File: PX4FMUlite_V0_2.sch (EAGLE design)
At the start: 148 parts, among them J201 DF13C-6P-1.25V, J202 DF13C-6P-1.25V, J203 DF13C-6P-1.25V, J204 DF13C-6P-1.25V, J301 47346-0001, J302 DF13C-4P-1.25V, J401 DF13C-4P-1.25V, J403 DF13C-7P-1.25V, J404 DF13C-5P-1.25V, J405 DF13C-4P-1.25V, J702 DF13C-3P-1.25V, J801 JST-ZH-3, M3_MOUNT1101 MOUNT-HOLE3.1MM, M3_MOUNT1102 MOUNT-HOLE3.1MM, M3_MOUNT1103 MOUNT-HOLE3.1MM, M3_MOUNT1104 MOUNT-HOLE3.1MM, U1 MPU-6000QFN-24, U101 STM32F4X7VX, U401 MAX3051, U903 74LVC2G240, X101 3.2x2.5 mm / 24 MHz / 15 ppm

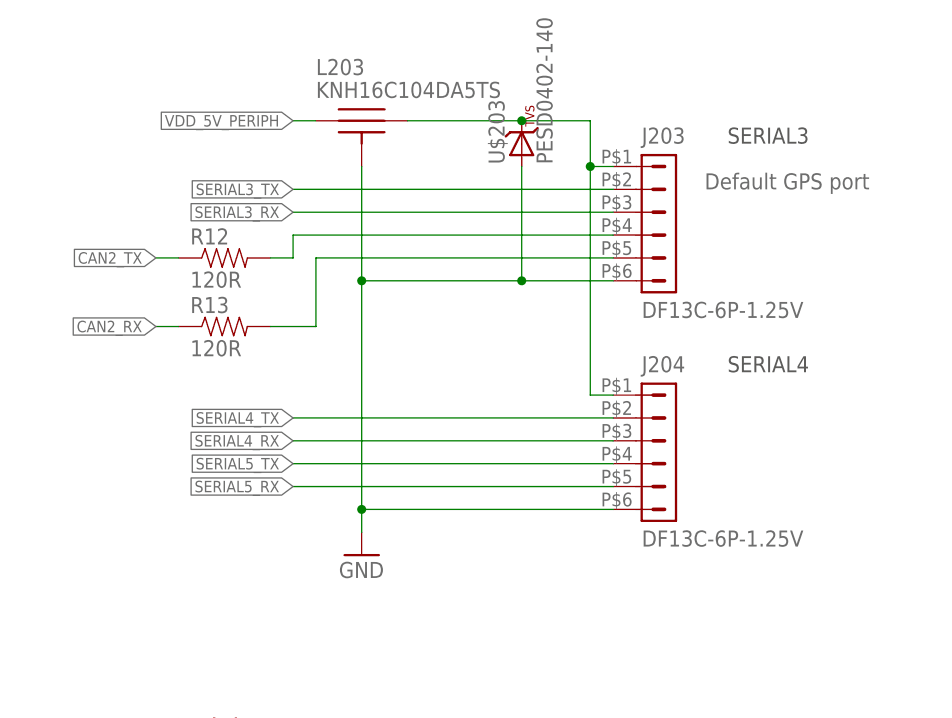
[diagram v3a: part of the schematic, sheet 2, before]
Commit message: Removed excess UART4/5 connector
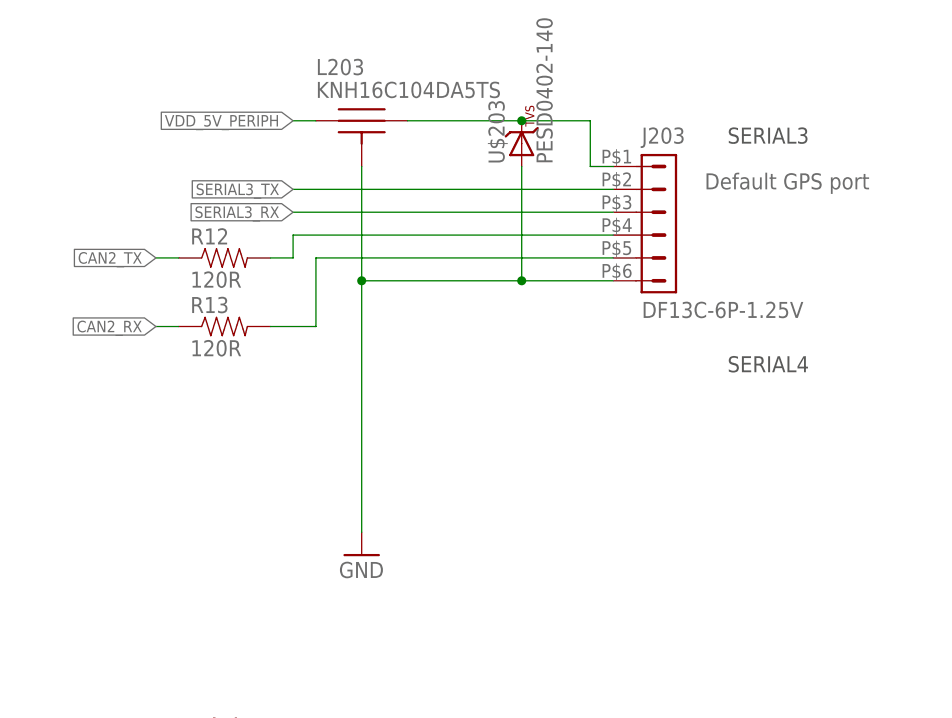
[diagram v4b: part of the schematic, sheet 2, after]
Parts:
- removed J204: DF13C-6P-1.25V, con-hirose-df13:DF13-6P-1.25V
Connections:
- net GNDX: no longer J204.6
- net N$100: no longer J204.1
- net SERIAL4_RX: no longer J204.3
- net SERIAL4_TX: no longer J204.2
- net SERIAL5_RX: no longer J204.5
- net SERIAL5_TX: no longer J204.4
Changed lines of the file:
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@@
-<attribute name="PARTNO" value="DF13C-6P-1.25V(20)"/>
-</part>
-<part name="J204" library="con-hirose-df13" deviceset="DF13-6P-1.25" device="V" value="DF13C-6P-1.25V">
 <attribute name="PARTNO" value="DF13C-6P-1.25V(20)"/>
 </part>
@@
 <attribute name="PARTNO" x="226.06" y="114.3" size="1.778" layer="96" display="off"/>
 </instance>
-<instance part="J204" gate="G$1" x="226.06" y="50.8">
-<attribute name="PARTNO" x="226.06" y="50.8" size="1.778" layer="96" display="off"/>
-</instance>
 <instance part="GND10" gate="1" x="193.04" y="38.1"/>
 <instance part="L201" gate="G$1" x="193.04" y="157.48">
@@
 <wire x1="220.98" y1="68.58" x2="210.82" y2="68.58" width="0.1524" layer="91"/>
 <pinref part="J203" gate="G$1" pin="6"/>
-<pinref part="J204" gate="G$1" pin="6"/>
 <wire x1="210.82" y1="68.58" x2="193.04" y2="68.58" width="0.1524" layer="91"/>
-<wire x1="220.98" y1="43.18" x2="193.04" y2="43.18" width="0.1524" layer="91"/>
-<wire x1="193.04" y1="68.58" x2="193.04" y2="43.18" width="0.1524" layer="91"/>
-<wire x1="193.04" y1="43.18" x2="193.04" y2="40.64" width="0.1524" layer="91"/>
+<wire x1="193.04" y1="68.58" x2="193.04" y2="40.64" width="0.1524" layer="91"/>
 <pinref part="GND10" gate="1" pin="GND"/>
-<junction x="193.04" y="43.18"/>
 <pinref part="L203" gate="G$1" pin="P$3"/>
 <wire x1="193.04" y1="68.58" x2="193.04" y2="81.28" width="0.1524" layer="91"/>
@@
 <net name="SERIAL4_TX" class="0">
 <segment>
-<wire x1="220.98" y1="53.34" x2="185.42" y2="53.34" width="0.1524" layer="91"/>
-<label x="185.42" y="53.34" size="1.27" layer="95" rot="R180" xref="yes"/>
-<pinref part="J204" gate="G$1" pin="2"/>
-</segment>
-<segment>
 <label x="124.46" y="48.26" size="1.27" layer="95" xref="yes"/>
 <pinref part="L3" gate="G$4" pin="P$2"/>
@@
 </net>
 <net name="SERIAL4_RX" class="0">
-<segment>
-<wire x1="220.98" y1="50.8" x2="185.42" y2="50.8" width="0.1524" layer="91"/>
-<label x="185.42" y="50.8" size="1.27" layer="95" rot="R180" xref="yes"/>
-<pinref part="J204" gate="G$1" pin="3"/>
-</segment>
 <segment>
 <label x="124.46" y="53.34" size="1.27" layer="95" xref="yes"/>
@@
 <net name="SERIAL5_TX" class="0">
 <segment>
-<pinref part="J204" gate="G$1" pin="4"/>
-<wire x1="220.98" y1="48.26" x2="185.42" y2="48.26" width="0.1524" layer="91"/>
-<label x="185.42" y="48.26" size="1.27" layer="95" rot="R180" xref="yes"/>
-</segment>
-<segment>
 <label x="124.46" y="58.42" size="1.27" layer="95" xref="yes"/>
 <pinref part="L3" gate="G$2" pin="P$2"/>
@@
 </net>
 <net name="SERIAL5_RX" class="0">
-<segment>
-<pinref part="J204" gate="G$1" pin="5"/>
-<wire x1="220.98" y1="45.72" x2="185.42" y2="45.72" width="0.1524" layer="91"/>
-<label x="185.42" y="45.72" size="1.27" layer="95" rot="R180" xref="yes"/>
-</segment>
 <segment>
 <label x="124.46" y="63.5" size="1.27" layer="95" xref="yes"/>
@@
 <wire x1="210.82" y1="86.36" x2="218.44" y2="86.36" width="0.1524" layer="91"/>
 <wire x1="218.44" y1="86.36" x2="218.44" y2="81.28" width="0.1524" layer="91"/>
-<pinref part="J204" gate="G$1" pin="1"/>
-<wire x1="218.44" y1="81.28" x2="218.44" y2="55.88" width="0.1524" layer="91"/>
-<wire x1="218.44" y1="55.88" x2="220.98" y2="55.88" width="0.1524" layer="91"/>
 <pinref part="J203" gate="G$1" pin="1"/>
 <wire x1="220.98" y1="81.28" x2="218.44" y2="81.28" width="0.1524" layer="91"/>
-<junction x="218.44" y="81.28"/>
 <pinref part="U$203" gate="G$1" pin="C"/>
 <junction x="210.82" y="86.36"/>

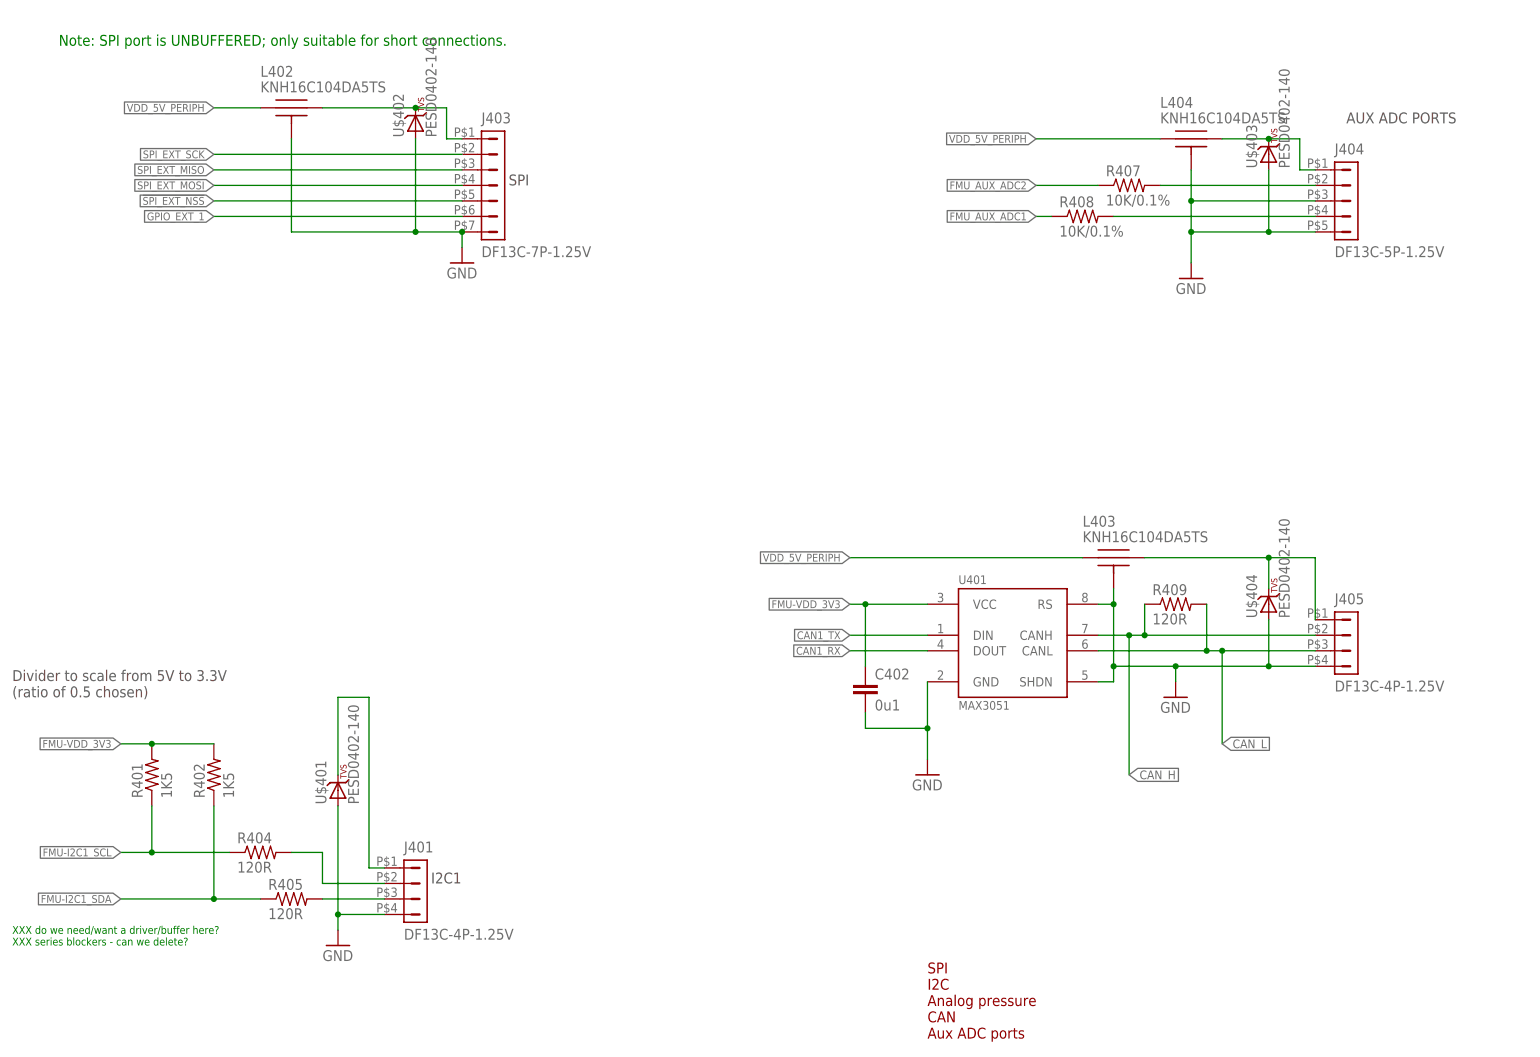
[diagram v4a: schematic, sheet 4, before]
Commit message: I2C2 connector added.
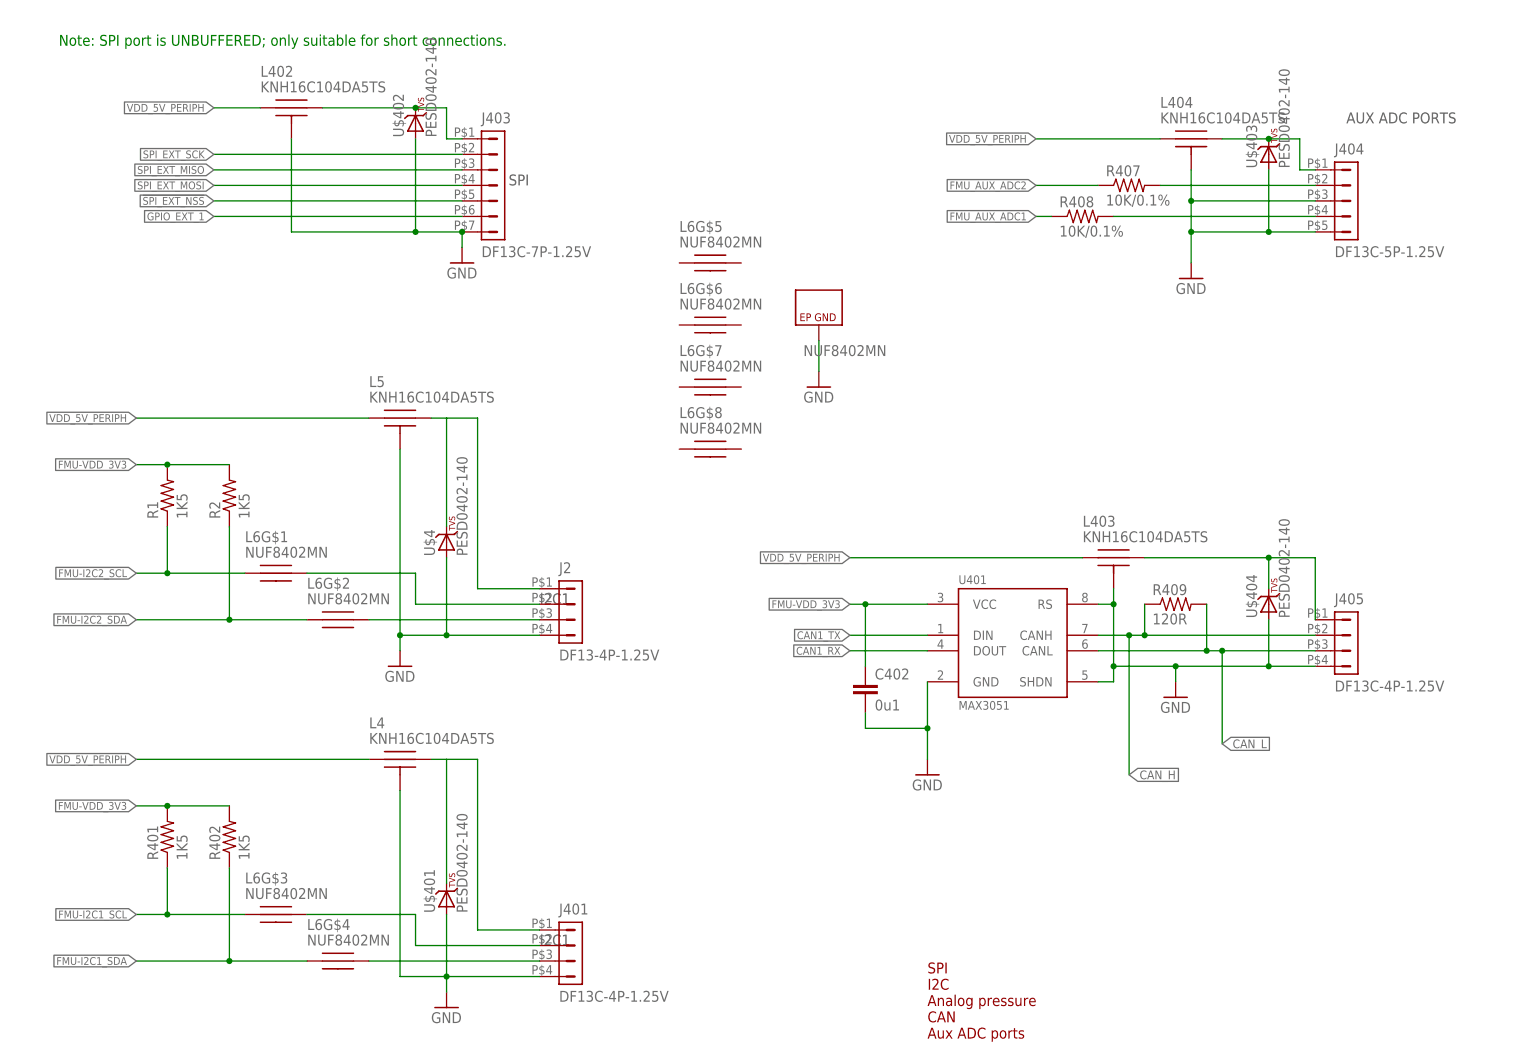
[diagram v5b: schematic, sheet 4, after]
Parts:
- removed R306, R307: 1K5, pixhawk2:RESISTOR0402-RES
- removed R404, R405: 120R, pixhawk2:RESISTOR0402-RES
- added J2: DF13-4P-1.25V, con-hirose-df13:DF13-4P-1.25V
- added L4, L5: KNH16C104DA5TS, pixhawk2:KNH16C104DA5TS
- added L6: NUF8402MN, PX4lite:NUF8402MN
- added R1, R2: 1K5, pixhawk2:RESISTOR0402-RES
- added U$4: PESD0402-140, pixhawk2:DIODE-TVS
- renumbered J702 to J802
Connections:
- new net N$20: J2.3, L6G$2.P$2
- new net N$21: J2.1, L5.P$2, U$4.C
- new net N$4: J2.2, L6G$1.P$2
- net FMU-I2C1_SCL: now also L6G$3.P$1; no longer R404.1
- net FMU-I2C1_SDA: now also L6G$4.P$1; no longer R405.1
- net FMU-I2C2_SCL: now also L6G$1.P$1, R1.1; no longer R306.1
- net FMU-I2C2_SDA: now also L6G$2.P$1, R2.1; no longer R307.1
- net FMU-VDD_3V3: now also R1.2, R2.2; no longer R306.2, R307.2
- net GND: now also J2.4, L5.P$3, U$4.A
- net GNDX: now also L4.P$3
- net N$33: now also L6G$3.P$2; no longer R404.2
- net N$37: now also L6G$4.P$2; no longer R405.2
- net N$42: now also L4.P$2
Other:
- note removed: "Divider to scale from 5V to 3.3V (ratio of 0.5 chosen)"
- note removed: "XXX do we need/want a driver/buffer here? XXX series blockers - can we delete?"
- moved on the sheet: J401, R401, R402, U$401

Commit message: General shuffling of filters
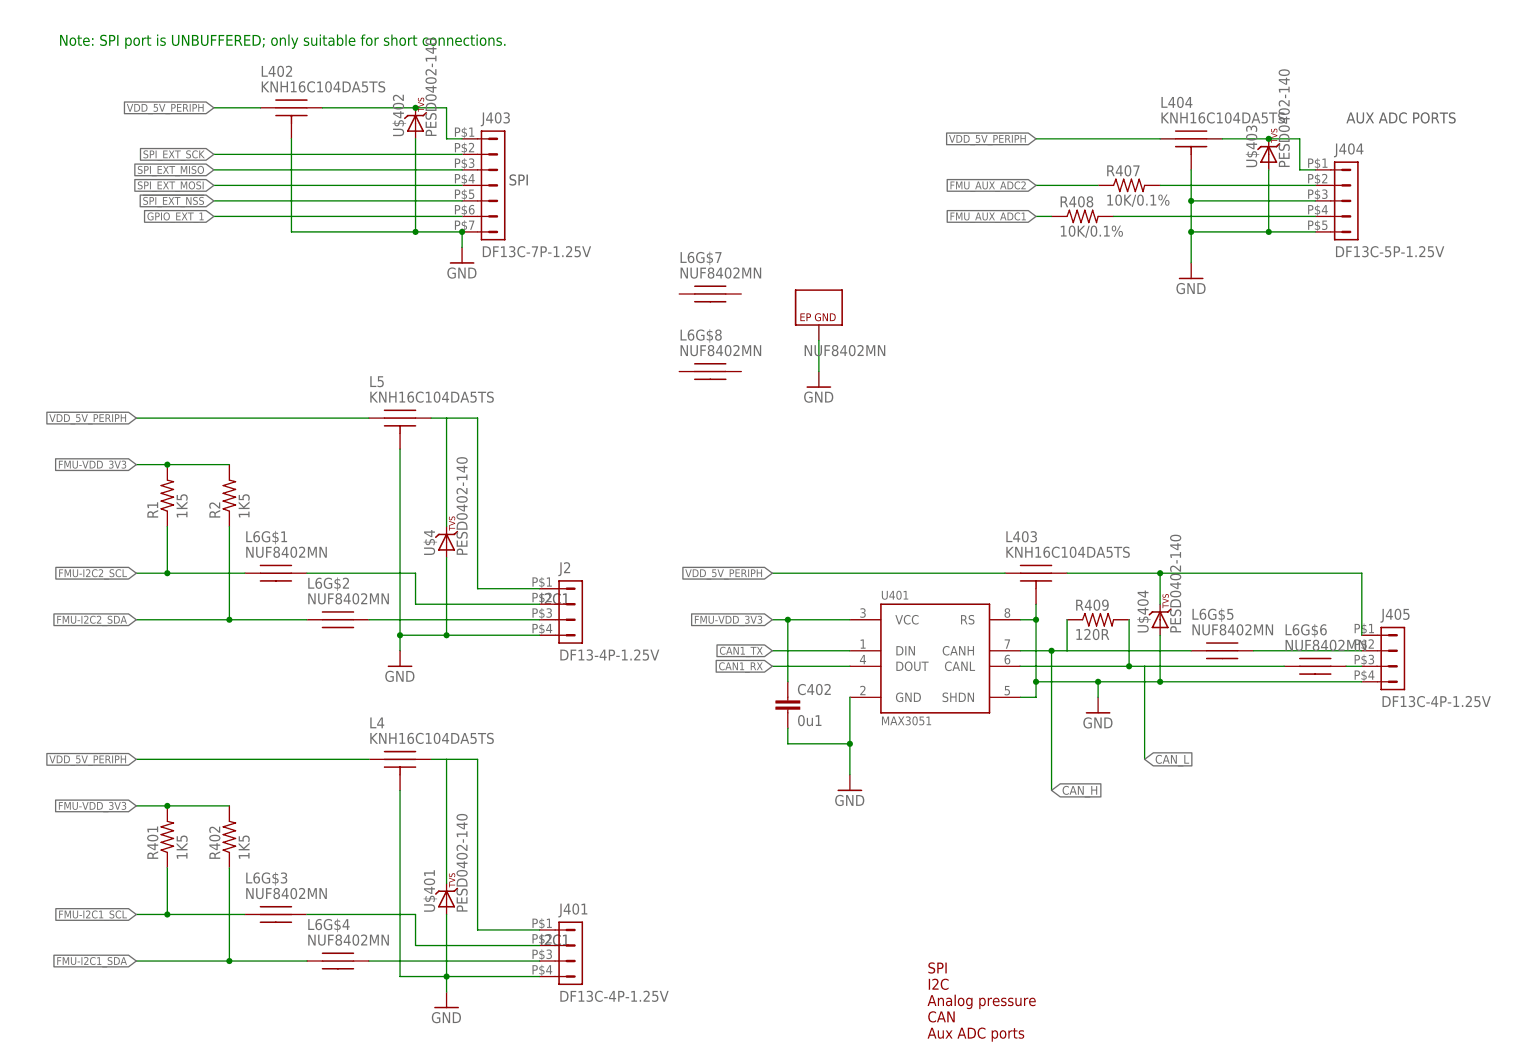
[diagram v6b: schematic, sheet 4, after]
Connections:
- new net N$22: J405.3, L6G$6.P$2
- new net N$24: J405.2, L6G$5.P$2
- net CAN_H: now also L6G$5.P$1; no longer J405.2
- net CAN_L: now also L6G$6.P$1; no longer J405.3
- net FMU-VDD_5V: now also LED701.A, LED704.A
- net VDD_5V_IN: no longer LED701.A, LED704.A
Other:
- note added: "USB Flash Expansion"
- note removed: "USB microSD Expansion"
- moved on the sheet: C402, J405, L403, L6G$5, L6G$6, L6G$7, L6G$8, R409, U$404, U401
